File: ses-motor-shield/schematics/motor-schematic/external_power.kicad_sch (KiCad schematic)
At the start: 21 parts, among them J1 EXTERNAL_MOTOR_POWER, J2 Conn_01x03_Female, Q2 TIP3055, U1 LM317_SOT-223, U4 AMS1117-5.0, U6 AMS1117-3.3

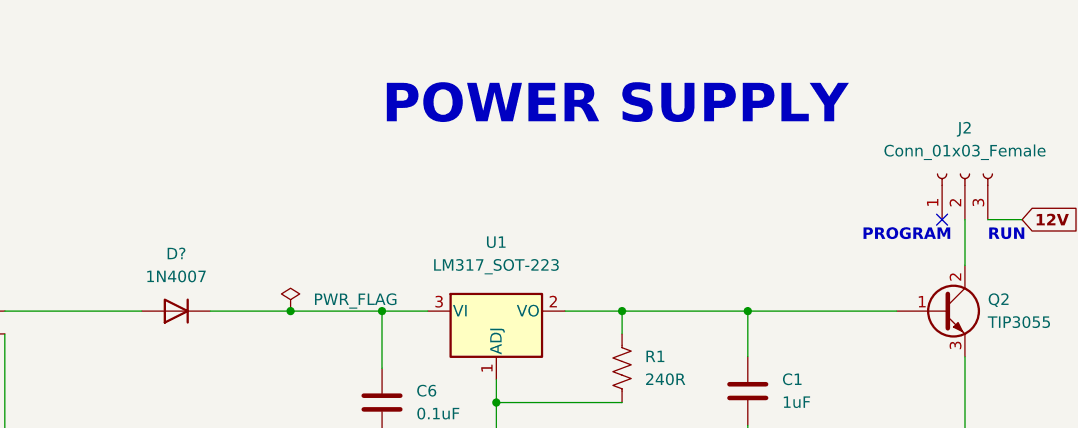
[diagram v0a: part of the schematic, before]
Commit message: created function overloading for servo
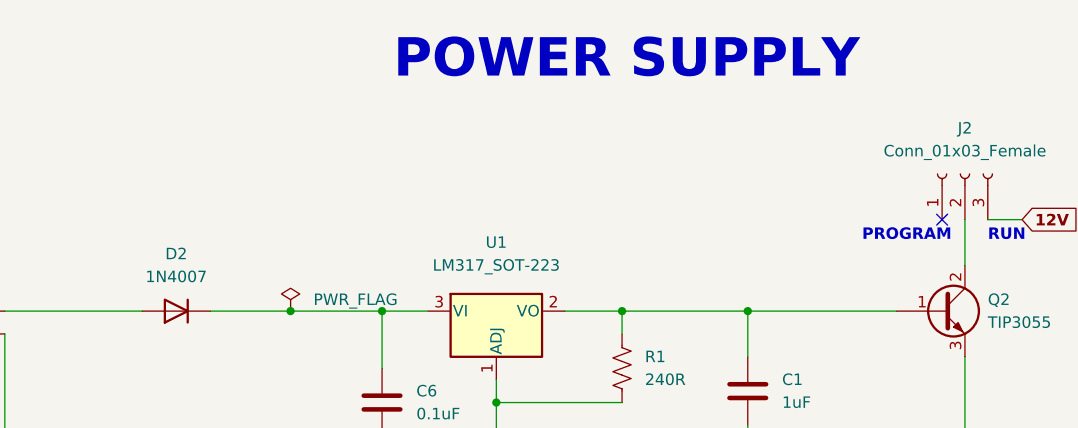
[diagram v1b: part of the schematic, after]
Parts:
- gave numbers to parts that had none: 1
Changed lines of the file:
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@@
     (effects (font (size 1.27 1.27) (thickness 0.254) bold) (justify left bottom))
   )
-  (text "POWER SUPPLY" (at 119.38 21.59 0)
+  (text "POWER SUPPLY" (at 120.65 16.51 0)
     (effects (font (size 4.27 4.27) bold) (justify left bottom))
   )
@@
   (symbol (lib_id "Diode:1N4007") (at 96.52 41.91 180) (unit 1)
     (in_bom yes) (on_board yes) (fields_autoplaced)
-    (property "Reference" "D?" (id 0) (at 96.52 35.56 0))
+    (property "Reference" "D2" (id 0) (at 96.52 35.56 0))
     (property "Value" "1N4007" (id 1) (at 96.52 38.1 0))
     (property "Footprint" "Diode_THT:D_DO-41_SOD81_P10.16mm_Horizontal" (id 2) (at 96.52 37.465 0)
